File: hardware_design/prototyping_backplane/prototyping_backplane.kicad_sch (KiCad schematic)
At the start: 18 parts, among them J1 BOOSTER_LEFT, J2 BOOSTER_RIGHT, J3 EXP_SPI, J4 EXP_LCD_CS, SW1 SW_DIP_x03, U1 TPS60204DGS

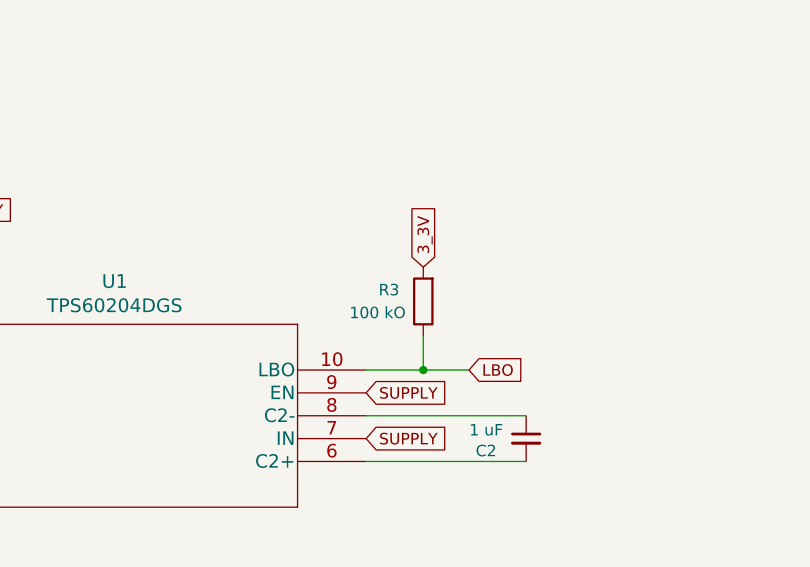
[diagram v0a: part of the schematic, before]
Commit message: Update schematics for revision D to close issue 35. PCB not complete, see release notes.
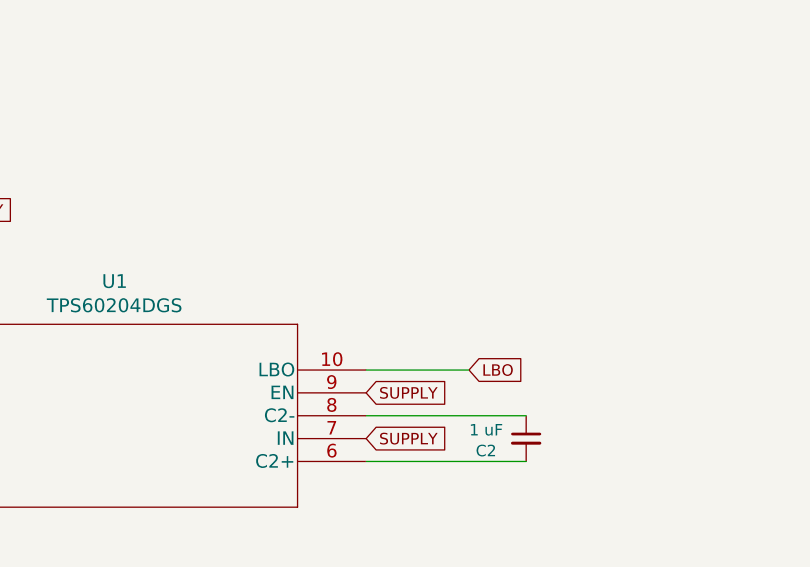
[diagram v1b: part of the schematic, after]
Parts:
- removed R3: 100 kO, Resistor_THT:R_Axial_DIN0204_L3.6mm_D1.6mm_P5.08mm_Horizontal, symbol Device:R
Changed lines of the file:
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@@
     (comment 1 "Not for resale model")
-  )
-  (junction (at 184.15 96.52) (diameter 0) (color 0 0 0 0)
   )
   (junction (at 97.79 106.68) (diameter 0) (color 0 0 0 0)
@@
     (stroke (width 0) (type default) (color 0 0 0 0))
   )
-  (wire (pts (xy 189.23 96.52) (xy 184.15 96.52))
+  (wire (pts (xy 177.8 96.52) (xy 189.23 96.52))
     (stroke (width 0) (type default) (color 0 0 0 0))
   )
@@
     (stroke (width 0) (type default) (color 0 0 0 0))
   )
-  (wire (pts (xy 184.15 96.52) (xy 177.8 96.52))
-    (stroke (width 0) (type default) (color 0 0 0 0))
-  )
   (wire (pts (xy 64.77 27.94) (xy 64.77 39.37))
     (stroke (width 0) (type default) (color 0 0 0 0))
@@
     (stroke (width 0) (type default) (color 0 0 0 0))
   )
-  (wire (pts (xy 184.15 92.71) (xy 184.15 96.52))
-    (stroke (width 0) (type default) (color 0 0 0 0))
-  )
   (wire (pts (xy 97.79 105.41) (xy 97.79 106.68))
     (stroke (width 0) (type default) (color 0 0 0 0))
@@
     (property "Intersheet References" "${INTERSHEET_REFS}" (id 0) (at 197.4891 142.1606 0)
       (effects (font (size 1.27 1.27)) (justify right) hide)
-    )
-  )
-  (global_label "3_3V" (shape input) (at 184.15 85.09 90) (fields_autoplaced)
-    (effects (font (size 1.27 1.27)) (justify left))
-    (property "Intersheet References" "${INTERSHEET_REFS}" (id 0) (at 184.0706 78.2906 90)
-      (effects (font (size 1.27 1.27)) (justify left) hide)
     )
   )
@@
     (pin "2")
   )
-  (symbol (lib_id "Device:R") (at 184.15 88.9 180) (unit 1)
-    (in_bom yes) (on_board yes)
-    (property "Reference" "R3" (id 0) (at 180.34 87.63 0))
-    (property "Value" "100 kO" (id 1) (at 179.07 90.17 0))
-    (property "Footprint" "Resistor_THT:R_Axial_DIN0204_L3.6mm_D1.6mm_P5.08mm_Horizontal" (id 2) (at 185.928 88.9 90)
-      (effects (font (size 1.27 1.27)) hide)
-    )
-    (property "Datasheet" "~" (id 3) (at 184.15 88.9 0)
-      (effects (font (size 1.27 1.27)) hide)
-    )
-    (pin "1")
-    (pin "2")
-  )
   (symbol (lib_id "Device:C_Small") (at 97.79 102.87 0) (unit 1)
     (in_bom yes) (on_board yes)
@@
       (reference "R2") (unit 1) (value "100 O") (footprint "Resistor_THT:R_Axial_DIN0207_L6.3mm_D2.5mm_P7.62mm_Horizontal")
     )
-    (path "/00000000-0000-0000-0000-00006375d8ee"
-      (reference "R3") (unit 1) (value "100 kO") (footprint "Resistor_THT:R_Axial_DIN0204_L3.6mm_D1.6mm_P5.08mm_Horizontal")
-    )
     (path "/00000000-0000-0000-0000-000063738c42"

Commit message: update/finalize revD backplanes
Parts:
- added Q1: 2N2222A, Package_TO_SOT_THT:TO-92, symbol Transistor_BJT:2N2219
- LS1: value Device Buzzer -> AST-02308MR-R; footprint Buzzer_Beeper:Buzzer_12x9.5RM7.6 -> footprints:Buzzer_D20mm_H7mm_P10mm
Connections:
- net 3_3V: now also Q1.3 (C)
- net BUZZER: now also Q1.2 (B); no longer LS1.1
- new net: LS1.1, Q1.1 (E)
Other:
- moved on the sheet: D1, D2, R1, R2
